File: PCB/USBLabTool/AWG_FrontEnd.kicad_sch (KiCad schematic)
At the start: 47 parts, among them J15 nuc303_LEFT, J16 nuc303_RIGHT, J17 USB_B, J18 2x01, J19 02x02, J20 BNC, J21 BNC, U7 Opamp_Quad, U8 Opamp_Quad, U9 DG403

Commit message: Starting PCB layout
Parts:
- removed J15: nuc303_LEFT, Connector_PinHeader_2.54mm:PinHeader_2x19_P2.54mm_Vertical, symbol awg_lib:nuc303_LEFT
- removed J16: nuc303_RIGHT, Connector_PinHeader_2.54mm:PinHeader_2x19_P2.54mm_Vertical, symbol awg_lib:nuc303_RIGHT
- removed J17: USB_B, Connector_USB:USB_B_Lumberg_2411_02_Horizontal, symbol Connector:USB_B
- removed JP1, JP2, JP5, JP6, JP7, JP8: JP, Jumper:SolderJumper-2_P1.3mm_Bridged_RoundedPad1.0x1.5mm, symbol Jumper:Jumper_2_Bridged
- removed R18, R19, R20, R31, R38, R40: 10K, Resistor_SMD:R_0603_1608Metric, symbol Device:R
- removed R24, R25: 22, Resistor_SMD:R_0603_1608Metric, symbol Device:R
- removed R26: 1K5, Resistor_SMD:R_0603_1608Metric, symbol Device:R
- removed unit 3 of U7
- removed unit 2 of U7
- removed unit 1 of U8
- removed unit 3 of U8
- removed unit 1 of U9
- added R1, R2, R3, R4, R5, R6: 10K, Resistor_SMD:R_0603_1608Metric, symbol Device:R
- added U1, U2: Opamp_Quad, Package_SO:SOIC-14W_7.5x9mm_P1.27mm, symbol Device:Opamp_Quad
- added U3: DG403, Package_SO:TSSOP-16-1EP_4.4x5mm_P0.65mm, symbol awg_lib:DG403
- J17: renamed from J18; footprint awg_fp_lib:1x02 -> Connector_PinHeader_2.54mm:PinHeader_2x01_P2.54mm_Vertical
- J18: renamed from J19; footprint awg_fp_lib:2x02 -> Connector_PinHeader_2.54mm:PinHeader_2x02_P2.54mm_Vertical
- TP3: footprint TestPoint:TestPoint_THTPad_1.5x1.5mm_Drill0.7mm -> TestPoint_THTPad_1.5x1.5mm_Drill0.7mm
- U10: renamed from U8; footprint awg_fp_lib:SOIC-14 -> Package_SO:SOIC-14W_7.5x9mm_P1.27mm
- U9: renamed from U7; footprint awg_fp_lib:SOIC-14 -> Package_SO:SOIC-14W_7.5x9mm_P1.27mm
- renumbered C23 to C29, C24 to C30, J20 to J19, J21 to J20, JP3 to JP1, JP4 to JP2, R21 to R36, R22 to R37, R23 to R38, R27 to R39, R28 to R40, R29 to R41, R30 to R42, R32 to R44, R33 to R45, R34 to R46, R35 to R47, R36 to R48, R37 to R49, R39 to R51, U9 to U12
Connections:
- net -5V: now also R1.2, R4.1
- net C0_FB: now also R4.2, U1.9 (-)
- net C0_IN: now also U1.5 (+)
- net C0_OUT_G: now also R5.2, U1.8
- net C1_FB: now also U3.16 (S1), U3.4 (S3)
- net C1_IN: now also U1.3 (+)
- net C1_OUT_GO: now also R2.2, U2.8
- net GND: now also U1.10 (+), U2.10 (+)
- net at JP2.2 (B), R38.1: now also U1.1, U1.2 (-)
- net at JP1.2 (B), R36.1: now also U1.6 (-), U1.7
- net at R41.1: now also U3.1 (D1)
- net at R42.2: now also U3.3 (D3)
- net at R44.2, R47.2, R48.1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: now also R5.1
- net at C29.1, U9.3 (+): now also R6.2
- net at C30.1, U10.5 (+): now also R3.2
- net at R45.2, R46.2, R49.2: now also R1.1, R2.1, U2.9 (-)
- net C0_S_GAIN renamed GAIN_C0
- new net GAIN_C1: U3.15 (IN1)
- new net TIM1_CH1: R6.1
- new net TIM1_CH2: R3.1
- no-connect marks 1 -> 0
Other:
- note added: "AWG CHAN 0"
- note added: "AWG CHAN 1"
- note added: "Switch U12A and U12B do not connect to U12C power source but KiCad will give false warnings if names are changed. DO NOT CONNECT THEM TOGETHER!!"
- note removed: "22ohm should be at the MCU pin not here, but we don't have a choice"
- note removed: "CHAN 0"
- note removed: "CHAN 1"
- note removed: "NO!"
- note removed: "YES"

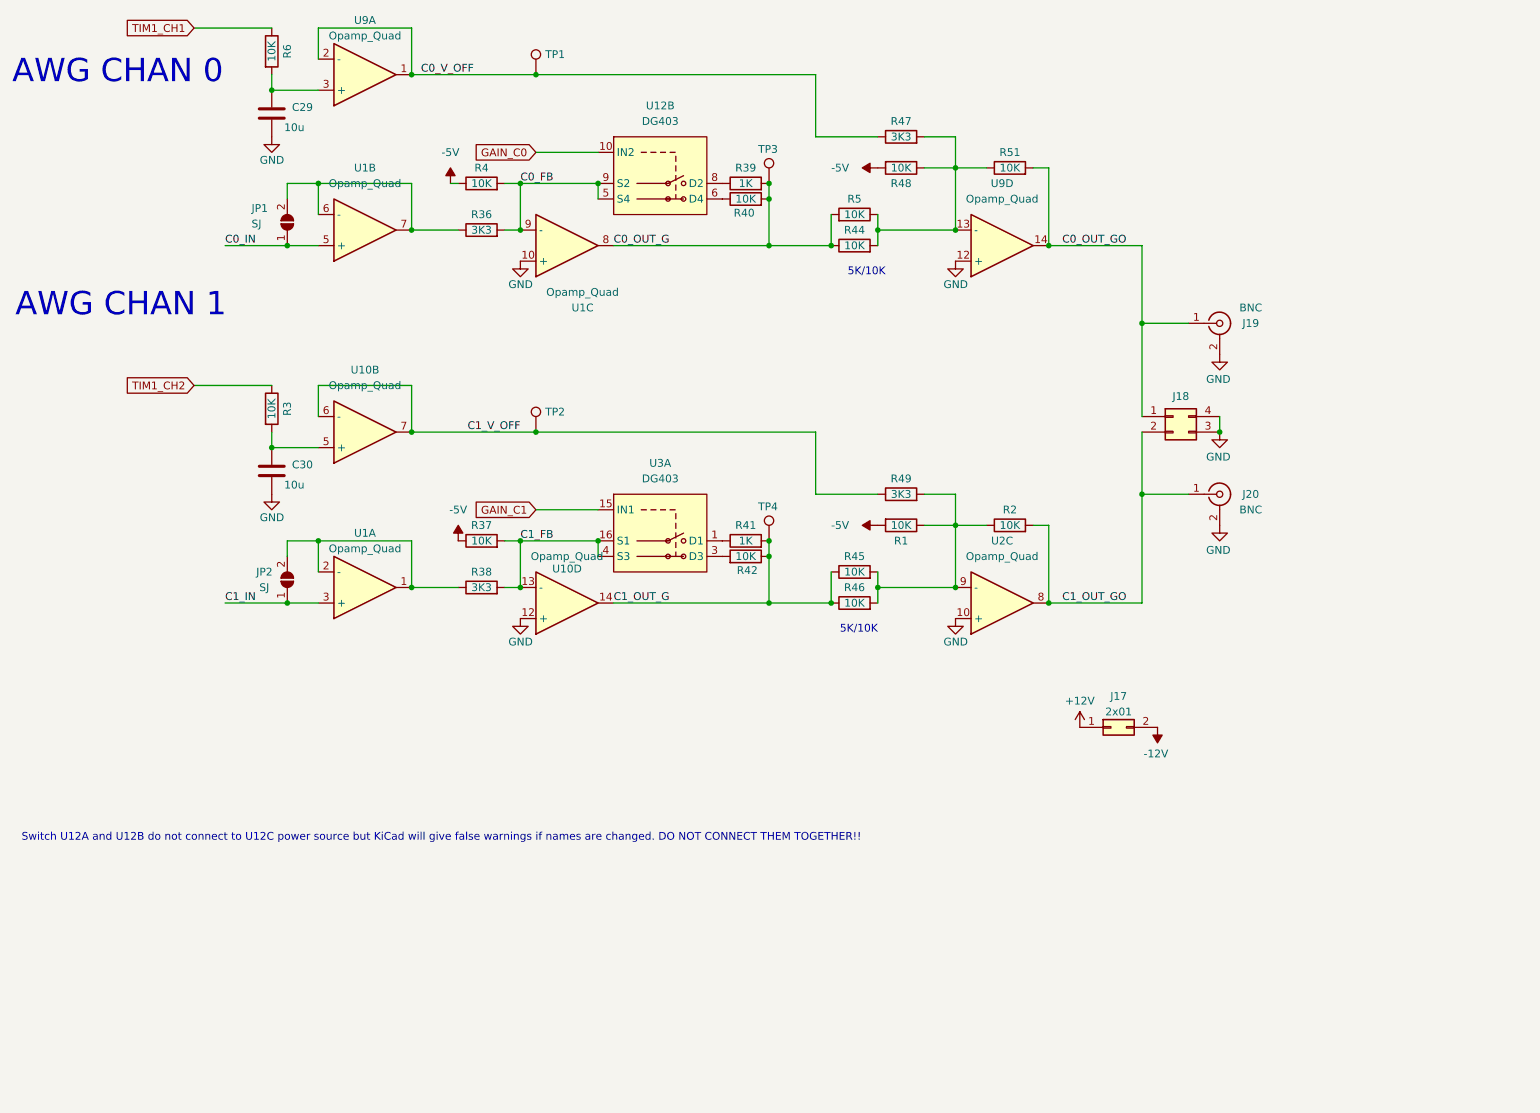
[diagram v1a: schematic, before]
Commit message: Moving files to where they should be
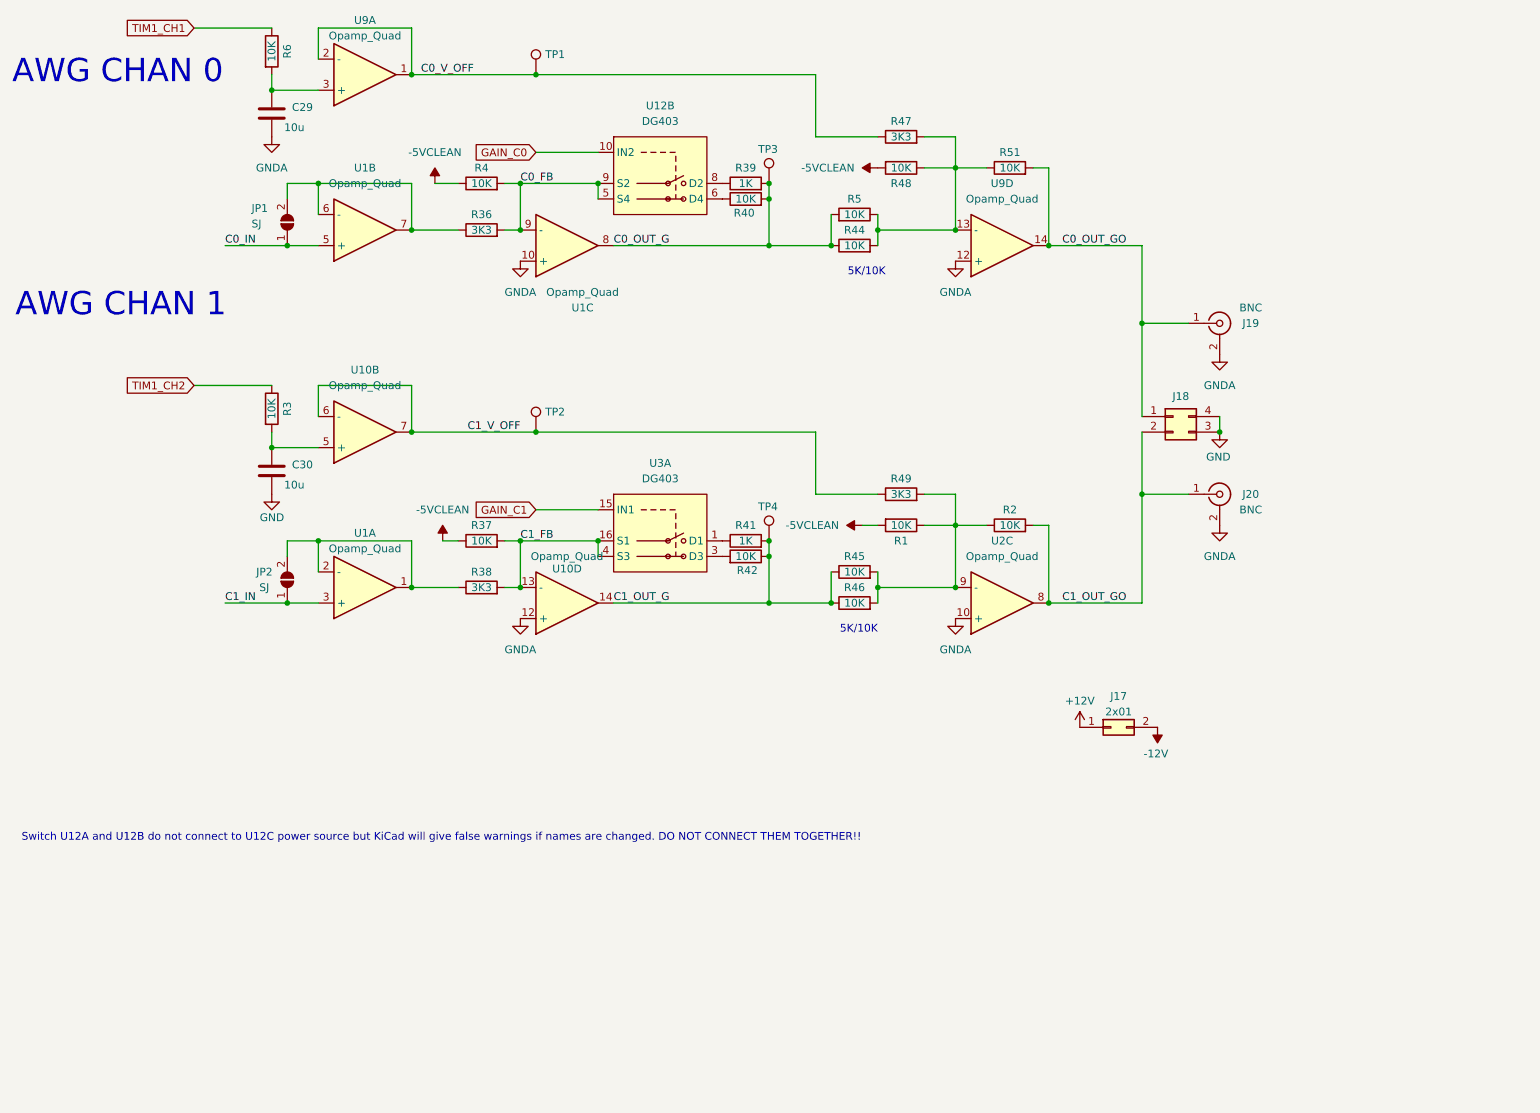
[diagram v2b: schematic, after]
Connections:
- net GND: no longer C29.2, J19.2 (Ext), J20.2 (Ext), U1.10 (+), U10.12 (+), U2.10 (+), U9.12 (+)
- net -5V renamed -5VCLEAN
- new net GNDA: C29.2, J19.2 (Ext), J20.2 (Ext), U1.10 (+), U10.12 (+), U2.10 (+), U9.12 (+)

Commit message: interim update (not done)
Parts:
- removed J19, J20: BNC, Connector_Coaxial:BNC_Amphenol_B6252HB-NPP3G-50_Horizontal, symbol Connector:Conn_Coaxial
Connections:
- net GND: no longer J18.3 (Pin_3), J18.4 (Pin_4)
- net GNDA: now also J18.3 (Pin_3), J18.4 (Pin_4)
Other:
- moved on the sheet: J17, JP1, JP2

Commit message: Routed revised PCB
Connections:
- net +12V renamed +12VA
- net -12V renamed -12VA
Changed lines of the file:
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@@
 			)
 		)
-		(property "Value" "-12V"
+		(property "Value" "-12VA"
 			(at 185.166 33.528 0)
 			(effects
@@
 			)
 		)
-		(property "Value" "+12V"
+		(property "Value" "+12VA"
 			(at 172.72 24.892 0)
 			(effects

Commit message: update MCU and USB, fix some footprints
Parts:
- renumbered U12 to U11
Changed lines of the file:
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@@
 		(dnp no)
 		(fields_autoplaced yes)
-		(property "Reference" "#PWR061"
+		(property "Reference" "#PWR062"
 			(at 152.4 43.18 0)
 			(effects
@@
 			(project "USBLabTool"
 				(path "/b5440f7d-90d5-417e-adc2-aa6b11e5424d/51eab4b3-0b2f-418c-9f7c-59af443ff2ad"
-					(reference "#PWR061")
+					(reference "#PWR062")
 					(unit 1)
 				)
@@
 			(project ""
 				(path "/b5440f7d-90d5-417e-adc2-aa6b11e5424d/51eab4b3-0b2f-418c-9f7c-59af443ff2ad"
-					(reference "U12")
+					(reference "U11")
 					(unit 1)
 				)
@@
 		(dnp no)
 		(fields_autoplaced yes)
-		(property "Reference" "U12"
+		(property "Reference" "U11"
 			(at 119.38 33.02 0)
 			(effects
@@
 			(project "USBLabTool"
 				(path "/b5440f7d-90d5-417e-adc2-aa6b11e5424d/51eab4b3-0b2f-418c-9f7c-59af443ff2ad"
-					(reference "U12")
+					(reference "U11")
 					(unit 2)
 				)
@@
 			(project "USBLabTool"
 				(path "/b5440f7d-90d5-417e-adc2-aa6b11e5424d/51eab4b3-0b2f-418c-9f7c-59af443ff2ad"
-					(reference "#PWR068")
+					(reference "#PWR067")
 					(unit 1)
 				)
@@
 		(dnp no)
 		(fields_autoplaced yes)
-		(property "Reference" "#PWR062"
+		(property "Reference" "#PWR061"
 			(at 149.86 101.6 0)
 			(effects
@@
 			(project "USBLabTool"
 				(path "/b5440f7d-90d5-417e-adc2-aa6b11e5424d/51eab4b3-0b2f-418c-9f7c-59af443ff2ad"
-					(reference "#PWR062")
-					(unit 1)
-				)
+					(reference "#PWR061")
+					(unit 1)
+				)

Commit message: modify MCU and name tags
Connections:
- net C0_OUT_GO renamed DAC1_OUT1
- net C1_OUT_GO renamed ADC2_INP7
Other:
- note added: "Will change this later on when connect them to a 20 pins"
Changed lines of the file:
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@@
+		)
+	)
+	(text "Will change this later on when connect them to a 20 pins\n"
+		(exclude_from_sim no)
+		(at 226.822 71.882 0)
+		(effects
+			(font
+				(size 1.27 1.27)
+			)
 		)
 	)
@@
 		)
 	)
+	(global_label "DAC1_OUT1"
+		(shape input)
+		(at 198.12 76.2 0)
+		(fields_autoplaced yes)
+		(effects
+			(font
+				(size 1.27 1.27)
+			)
+			(justify left)
+		)
+		(property "Intersheetrefs" "${INTERSHEET_REFS}"
+			(at 211.749 76.2 0)
+			(effects
+				(font
+					(size 1.27 1.27)
+				)
+				(justify left)
+				(hide yes)
+			)
+		)
+	)
 	(global_label "GAIN_C1"
 		(shape input)
@@
 				(hide yes)
 			)
+		)
+	)
+	(global_label "ADC2_INP7"
+		(shape input)
+		(at 198.12 95.25 0)
+		(fields_autoplaced yes)
+		(effects
+			(font
+				(size 1.27 1.27)
+			)
+			(justify left)
+		)
+		(property "Intersheetrefs" "${INTERSHEET_REFS}"
+			(at 211.3257 95.25 0)
+			(effects
+				(font
+					(size 1.27 1.27)
+				)
+				(justify left)
+				(hide yes)
+			)

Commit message: add NRST button and change MCU pins as latest
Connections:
- net ADC2_INP7 renamed DAC1_OUT2
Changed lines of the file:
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@@
+		)
+	)
+	(global_label "DAC1_OUT2"
+		(shape input)
+		(at 198.12 93.98 0)
+		(fields_autoplaced yes)
+		(effects
+			(font
+				(size 1.27 1.27)
+			)
+			(justify left)
+		)
+		(property "Intersheetrefs" "${INTERSHEET_REFS}"
+			(at 211.749 93.98 0)
+			(effects
+				(font
+					(size 1.27 1.27)
+				)
+				(justify left)
+				(hide yes)
+			)
 		)
 	)
@@
 				(hide yes)
 			)
-		)
-	)
-	(global_label "ADC2_INP7"
-		(shape input)
-		(at 198.12 95.25 0)
-		(fields_autoplaced yes)
-		(effects
-			(font
-				(size 1.27 1.27)
-			)
-			(justify left)
-		)
-		(property "Intersheetrefs" "${INTERSHEET_REFS}"
-			(at 211.3257 95.25 0)
-			(effects
-				(font
-					(size 1.27 1.27)
-				)
-				(justify left)
-				(hide yes)
-			)
